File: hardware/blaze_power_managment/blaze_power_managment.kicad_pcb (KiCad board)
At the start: 4 copper layers, 70 x 70 mm, 64 parts, among them J1 FrontInterconnect, J2 RearInterconnect, J3 XT30, J4 XT30, J5 JTAG, Q1 DMG2305, SW1 SW_SPST, SW2 SW_SPDT, U1 TCAN1044VDDFR, U2 TPS62913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

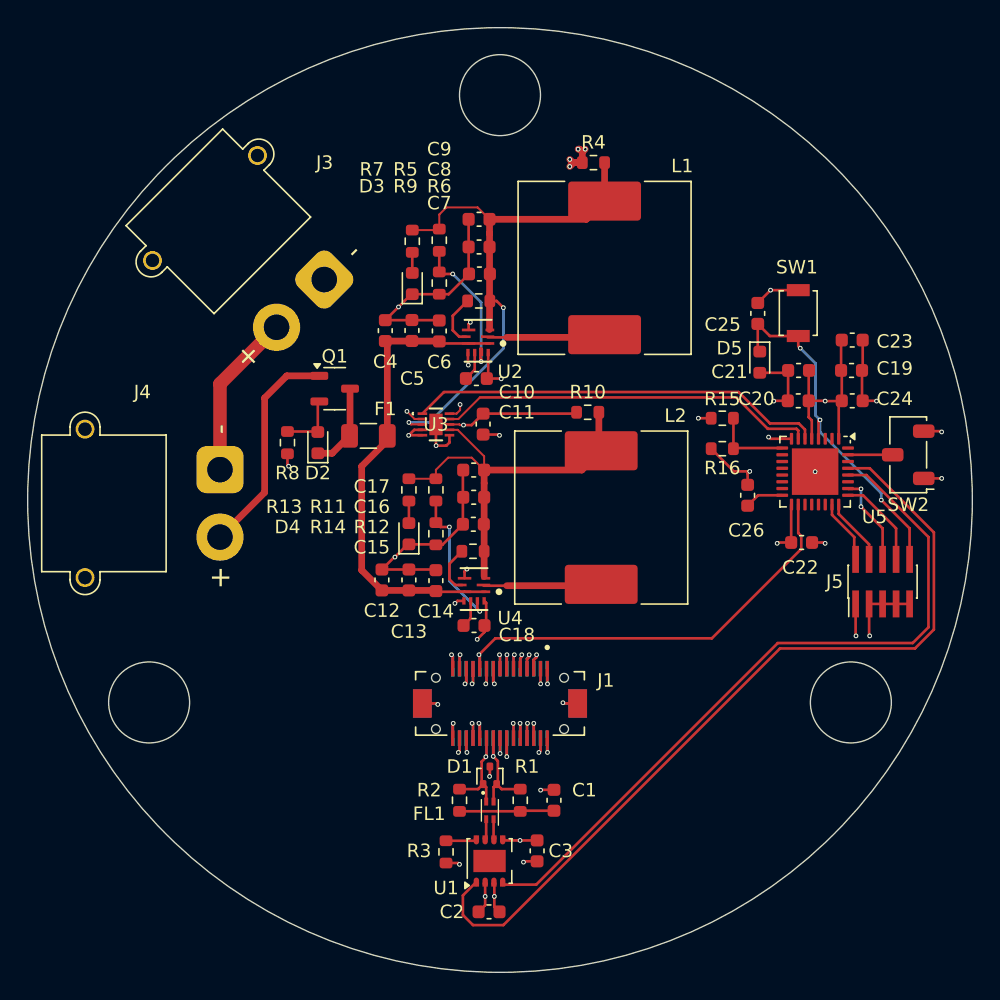
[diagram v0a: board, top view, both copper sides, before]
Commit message: Added Fillets
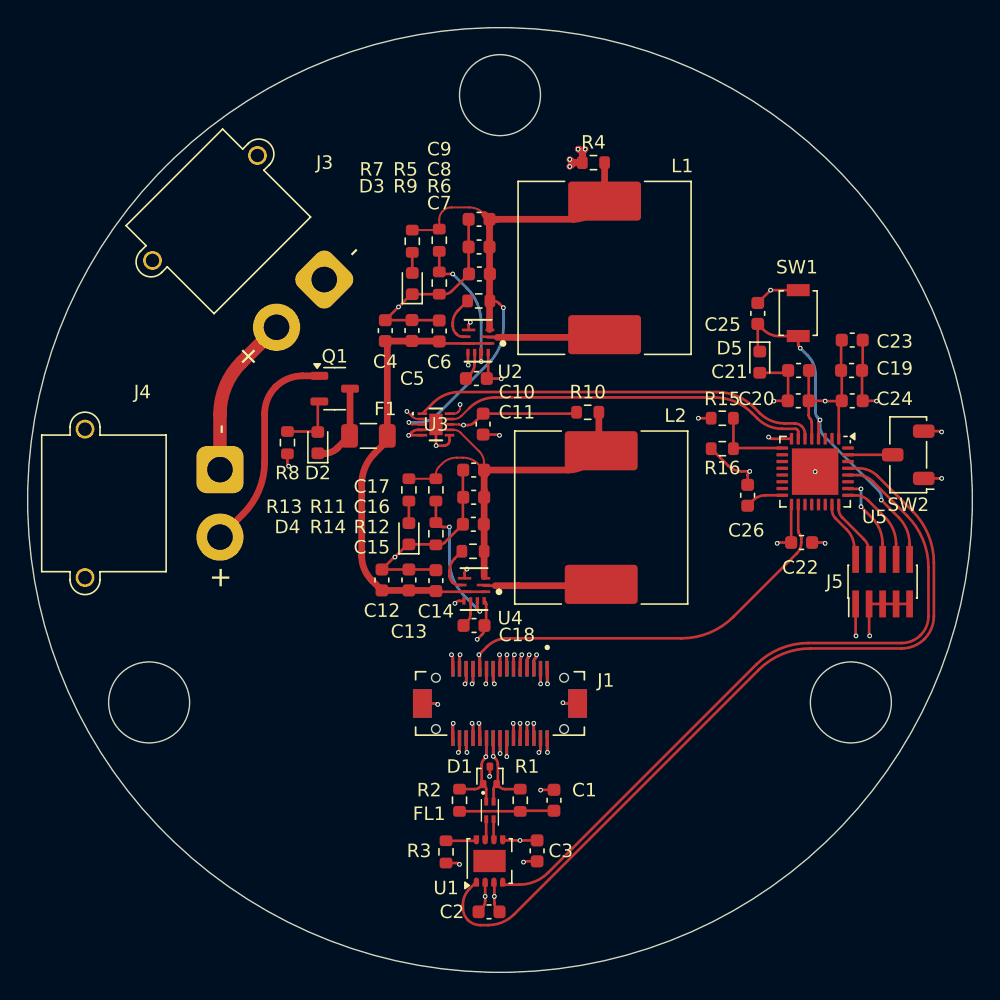
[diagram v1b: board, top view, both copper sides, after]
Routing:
- net /CANTX: track 62.7 -> 61.5 mm
- net /CANRX: track 54.0 -> 53.1 mm
- net GND: track 98.1 -> 97.3 mm
- net /3V3_SENSE_IN: track 31.5 -> 30.8 mm
- net Net-(J4-Pin_2): track 16.4 -> 15.9 mm
- net /3V3_SENSE: track 30.8 -> 30.3 mm
- net /5V_SENSE_IN: track 42.3 -> 42.8 mm
- net /5V_SENSE: track 28.1 -> 27.6 mm

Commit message: Silkscreen Update
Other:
- board text added: "Blaze PowerMan v1 UCSC Rocket Team 2025"
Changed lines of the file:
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@@
 			(layer "F.Fab")
 		)
-		(fp_text user "+"
-			(at -8 0 90)
-			(layer "F.SilkS")
-			(effects
-				(font
-					(size 1.5 1.5)
-					(thickness 0.15)
-				)
-			)
-		)
-		(fp_text user "-"
-			(at 3 0 90)
-			(layer "F.SilkS")
-			(effects
-				(font
-					(size 1.5 1.5)
-					(thickness 0.15)
-				)
-			)
-		)
 		(fp_text user "${REFERENCE}"
 			(at -2.5 -3 90)
@@
 		(layer "Edge.Cuts")
 	)
+	(gr_text "Blaze PowerMan v1\nUCSC Rocket Team\n2025"
+		(at 155.321 129.667 0)
+		(layer "B.SilkS")
+		(effects
+			(font
+				(size 1 1)
+				(thickness 0.1)
+			)
+			(justify left bottom mirror)
+		)
+	)
 	(dimension
